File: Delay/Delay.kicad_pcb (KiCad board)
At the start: 2 copper layers, 60 x 110 mm, 64 parts, among them J1 IN, J2 DC IN, J3 OUT, U1 TL072, U2 PT2399, U3 LP2950-5.0_TO252

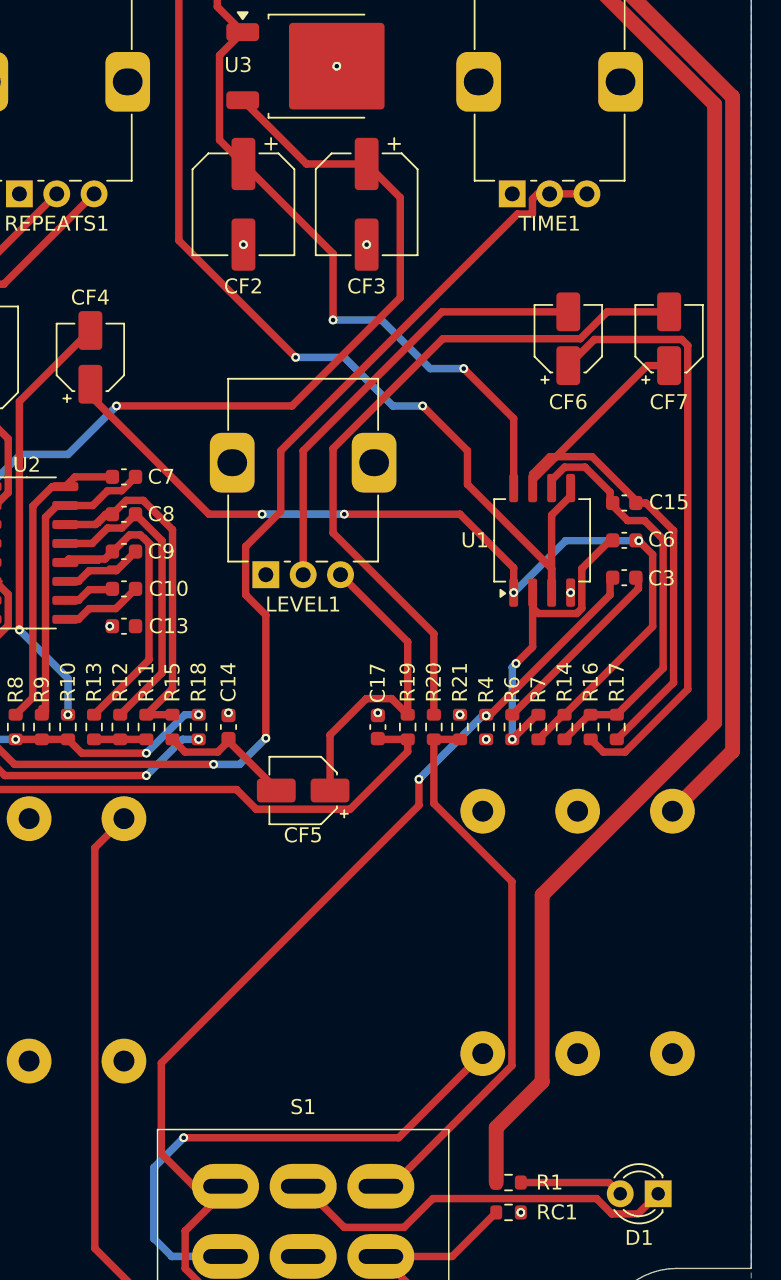
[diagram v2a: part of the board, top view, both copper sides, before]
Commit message: moved input jack to match the x height of the output jack (it was off by 0.5mm)
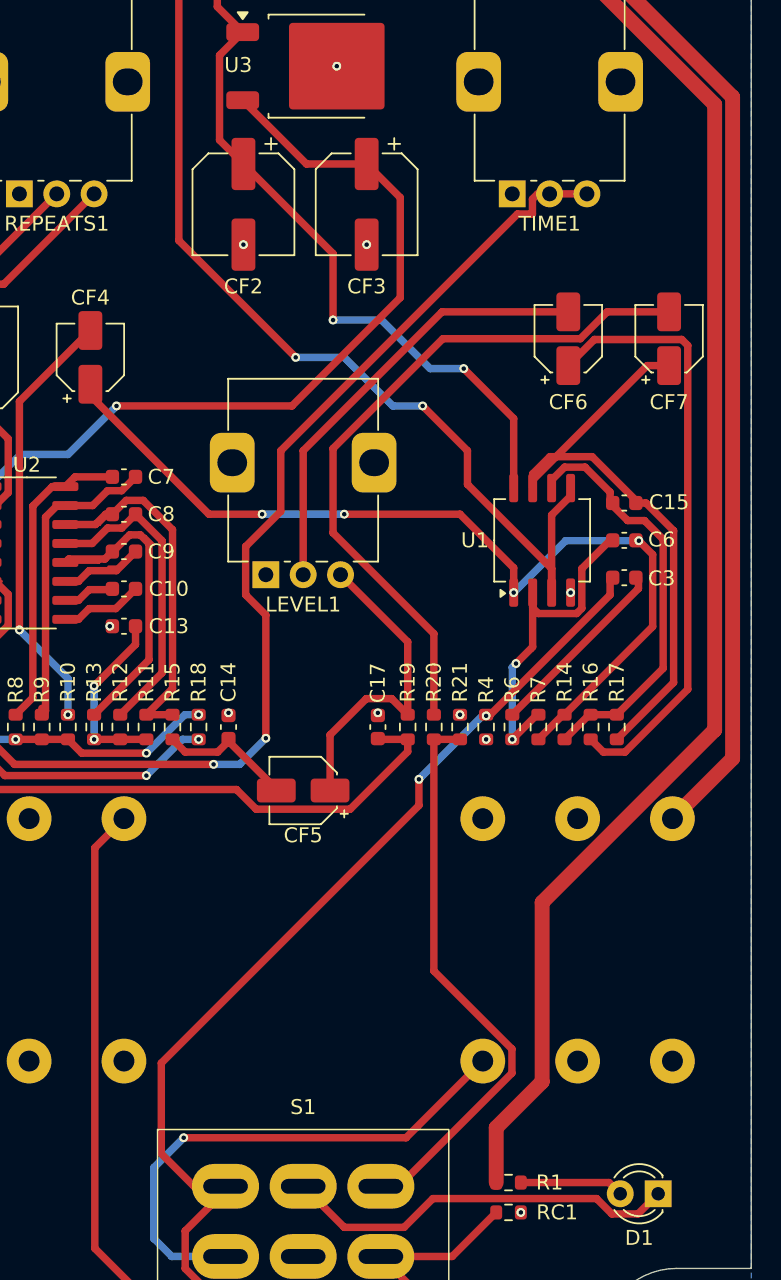
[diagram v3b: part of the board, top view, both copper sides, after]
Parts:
- moved J1 0.50 mm to (162.0, 126.1)
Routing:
- net Net-(C13-Pad1): track 3.50 -> 12.2 mm, vias 0 -> 2
- net Net-(-9VBATT1-Pad1): track 74.2 -> 75.2 mm
- net Wet Out: track 37.2 -> 38.2 mm
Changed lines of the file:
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@@
 	(footprint "Connector_Audio:Jack_6.35mm_Neutrik_NMJ6HFD2_Horizontal"
 		(layer "B.Cu")
-		(at 162.025 125.615)
+		(at 162.025 126.115)
 		(descr "M Series, 6.35mm (1/4in) stereo jack, switched, with full threaded nose and straight PCB pins, https://www.neutrik.com/en/product/nmj6hfd2")
 		(tags "neutrik jack m")
@@
 	)
 	(segment
-		(start 177.551 103.446315)
-		(end 177.551 62.067848)
-		(width 1)
-		(layer "F.Cu")
-		(net 1)
-	)
-	(segment
 		(start 139.999 48.447292)
 		(end 139.999 46.026)
@@
 	)
 	(segment
-		(start 166 127.5)
-		(end 166 114.997315)
-		(width 1)
-		(layer "F.Cu")
-		(net 1)
-	)
-	(segment
 		(start 141.025 45)
 		(end 141.025 42.425)
 		(width 0.5)
+		(layer "F.Cu")
+		(net 1)
+	)
+	(segment
+		(start 153.001 48.551)
+		(end 150 45.55)
+		(width 1)
 		(layer "F.Cu")
 		(net 1)
@@
 	)
 	(segment
+		(start 150 45.55)
+		(end 145.649 41.199)
+		(width 0.5)
+		(layer "F.Cu")
+		(net 1)
+	)
+	(segment
+		(start 139.999 46.026)
+		(end 141.025 45)
+		(width 0.5)
+		(layer "F.Cu")
+		(net 1)
+	)
+	(segment
+		(start 150 45.55)
+		(end 144.25 51.3)
+		(width 0.5)
+		(layer "F.Cu")
+		(net 1)
+	)
+	(segment
 		(start 154.095423 51.751)
 		(end 153.001 50.656577)
@@
 	)
 	(segment
-		(start 150 45.55)
-		(end 145.649 41.199)
-		(width 0.5)
-		(layer "F.Cu")
-		(net 1)
-	)
-	(segment
-		(start 139.999 46.026)
-		(end 141.025 45)
-		(width 0.5)
-		(layer "F.Cu")
-		(net 1)
-	)
-	(segment
-		(start 150 45.55)
-		(end 144.25 51.3)
-		(width 0.5)
+		(start 177.551 62.067848)
+		(end 167.234152 51.751)
+		(width 1)
 		(layer "F.Cu")
 		(net 1)
@@
 		(start 145.649 41.199)
 		(end 141.901 41.199)
-		(width 0.5)
-		(layer "F.Cu")
-		(net 1)
-	)
-	(segment
-		(start 141.051708 49.5)
-		(end 139.999 48.447292)
 		(width 0.5)
 		(layer "F.Cu")
@@
 	)
 	(segment
+		(start 141.051708 49.5)
+		(end 139.999 48.447292)
+		(width 0.5)
+		(layer "F.Cu")
+		(net 1)
+	)
+	(segment
+		(start 177.551 103.946315)
+		(end 166 115.497315)
+		(width 1)
+		(layer "F.Cu")
+		(net 1)
+	)
+	(segment
 		(start 162.925 134.25)
 		(end 162.925 130.575)
@@
 	)
 	(segment
-		(start 166 114.997315)
-		(end 177.551 103.446315)
+		(start 166 115.497315)
+		(end 166 127.5)
 		(width 1)
 		(layer "F.Cu")
@@
 		(start 144.25 51.3)
 		(end 144.25 55.52)
+		(width 0.5)
+		(layer "F.Cu")
+		(net 1)
+	)
+	(segment
+		(start 177.551 62.067848)
+		(end 177.551 103.946315)
+		(width 1)
+		(layer "F.Cu")
+		(net 1)
+	)
+	(segment
+		(start 164.095 87.75)
+		(end 164.095 83.095)
 		(width 0.5)
 		(layer "F.Cu")
@@
 		(net 1)
 	)
-	(segment
-		(start 177.551 62.067848)
-		(end 167.234152 51.751)
-		(width 1)
-		(layer "F.Cu")
-		(net 1)
-	)
-	(segment
-		(start 164.095 87.75)
-		(end 164.095 83.095)
-		(width 0.5)
-		(layer "F.Cu")
-		(net 1)
-	)
-	(segment
-		(start 153.001 48.551)
-		(end 150 45.55)
-		(width 1)
-		(layer "F.Cu")
-		(net 1)
-	)
 	(via
 		(at 160.75 79.75)
@@
 	)
 	(segment
-		(start 156.39 131.25)
-		(end 162.025 125.615)
+		(start 156.89 131.25)
+		(end 162.025 126.115)
 		(width 0.5)
 		(layer "F.Cu")
@@
 	(segment
 		(start 142 131.25)
-		(end 156.39 131.25)
+		(end 156.89 131.25)
 		(width 0.5)
 		(layer "F.Cu")
@@
 	)
 	(segment
-		(start 163.976 126.423131)
-		(end 163.976 114.095131)
+		(start 163.976 125.306869)
+		(end 163.976 126.923131)
 		(width 0.5)
 		(layer "F.Cu")
@@
 	)
 	(segment
-		(start 158.75 108.869131)
-		(end 158.75 104.575)
+		(start 163.976 126.923131)
+		(end 156.399131 134.5)
 		(width 0.5)
 		(layer "F.Cu")
@@
 	)
 	(segment
-		(start 163.976 114.095131)
-		(end 158.75 108.869131)
+		(start 158.75 104.575)
+		(end 158.75 120.080869)
+		(width 0.5)
+		(layer "F.Cu")
+		(net 9)
+	)
+	(segment
+		(start 156.399131 134.5)
+		(end 155.2 134.5)
+		(width 0.5)
+		(layer "F.Cu")
+		(net 9)
+	)
+	(segment
+		(start 158.75 120.080869)
+		(end 163.976 125.306869)
 		(width 0.5)
 		(layer "F.Cu")
@@
 	)
 	(segment
-		(start 155.899131 134.5)
-		(end 163.976 126.423131)
-		(width 0.5)
-		(layer "F.Cu")
-		(net 9)
-	)
-	(segment
 		(start 146.751 145.851)
 		(end 144.8 143.9)
@@
 	)
 	(segment
+		(start 138.775 98.225)
+		(end 138.775 97)
+		(width 0.5)
+		(layer "F.Cu")
+		(net 13)
+	)
+	(segment
+		(start 136 101)
+		(end 138.775 98.225)
+		(width 0.5)
+		(layer "F.Cu")
+		(net 13)
+	)
+	(segment
 		(start 136 104.575)
 		(end 139.5 104.575)
 		(width 0.5)
 		(layer "F.Cu")
+		(net 13)
+	)
+	(via
+		(at 136 104.575)
+		(size 0.6)
+		(drill 0.3)
+		(layers "F.Cu" "B.Cu")
+		(net 13)
+	)
+	(via
+		(at 136 101)
+		(size 0.6)
+		(drill 0.3)
+		(layers "F.Cu" "B.Cu")
+		(net 13)
+	)
+	(segment
+		(start 136 104.575)
+		(end 136 101)
+		(width 0.5)
+		(layer "B.Cu")
 		(net 13)
 	)
@@
 	)
 	(segment
+		(start 174.725 109.385)
+		(end 174.725 109.885)
+		(width 1)
+		(layer "F.Cu")
+		(net 22)
+	)
+	(segment
+		(start 178.752 61.570378)
+		(end 178.752 105.858)
+		(width 1)
+		(layer "F.Cu")
+		(net 22)
+	)
+	(segment
 		(start 159.25 49)
 		(end 166.181622 49)
@@
 	)
 	(segment
-		(start 178.752 61.570378)
-		(end 178.752 105.358)
+		(start 178.752 105.858)
+		(end 174.725 109.885)
 		(width 1)
 		(layer "F.Cu")
-		(net 22)
-	)
-	(segment
-		(start 178.752 105.358)
-		(end 174.725 109.385)
-		(width 1)
-		(layer "F.Cu")

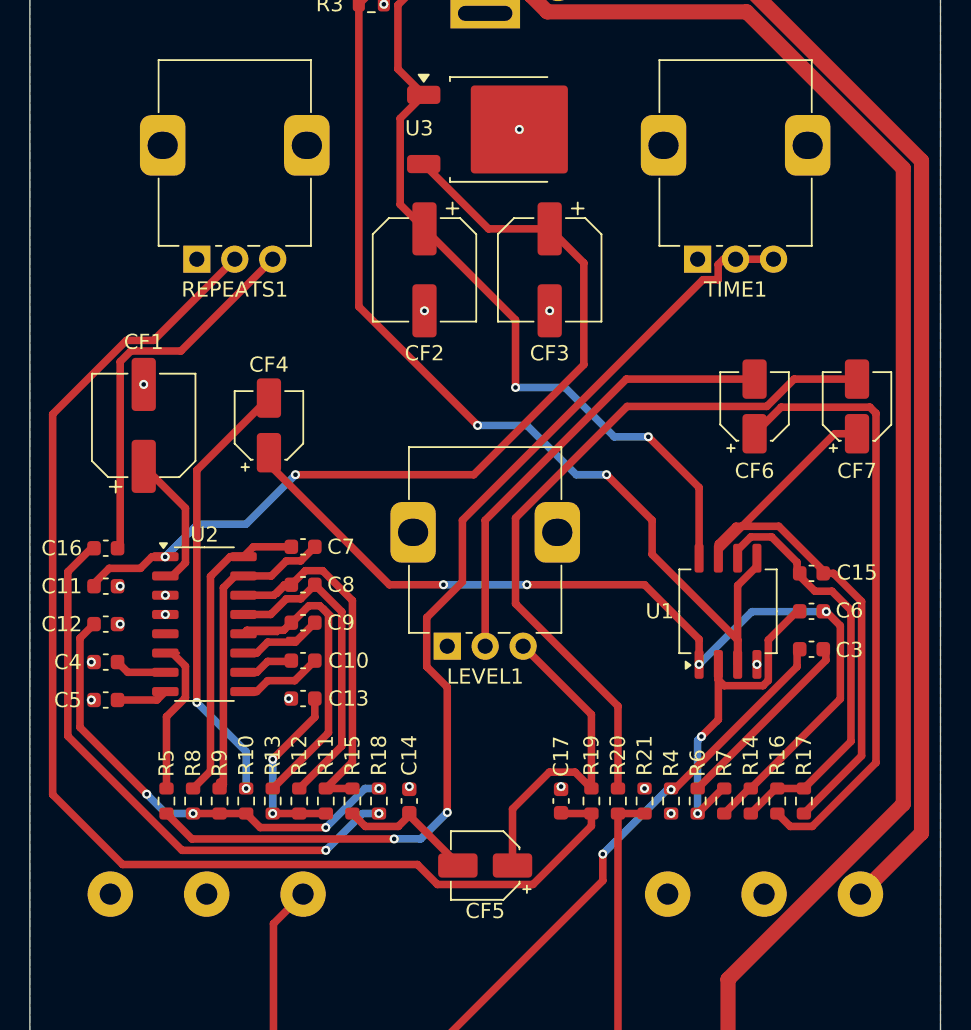
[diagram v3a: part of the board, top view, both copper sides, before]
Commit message: changed caps to be THT and to be sourced separately.
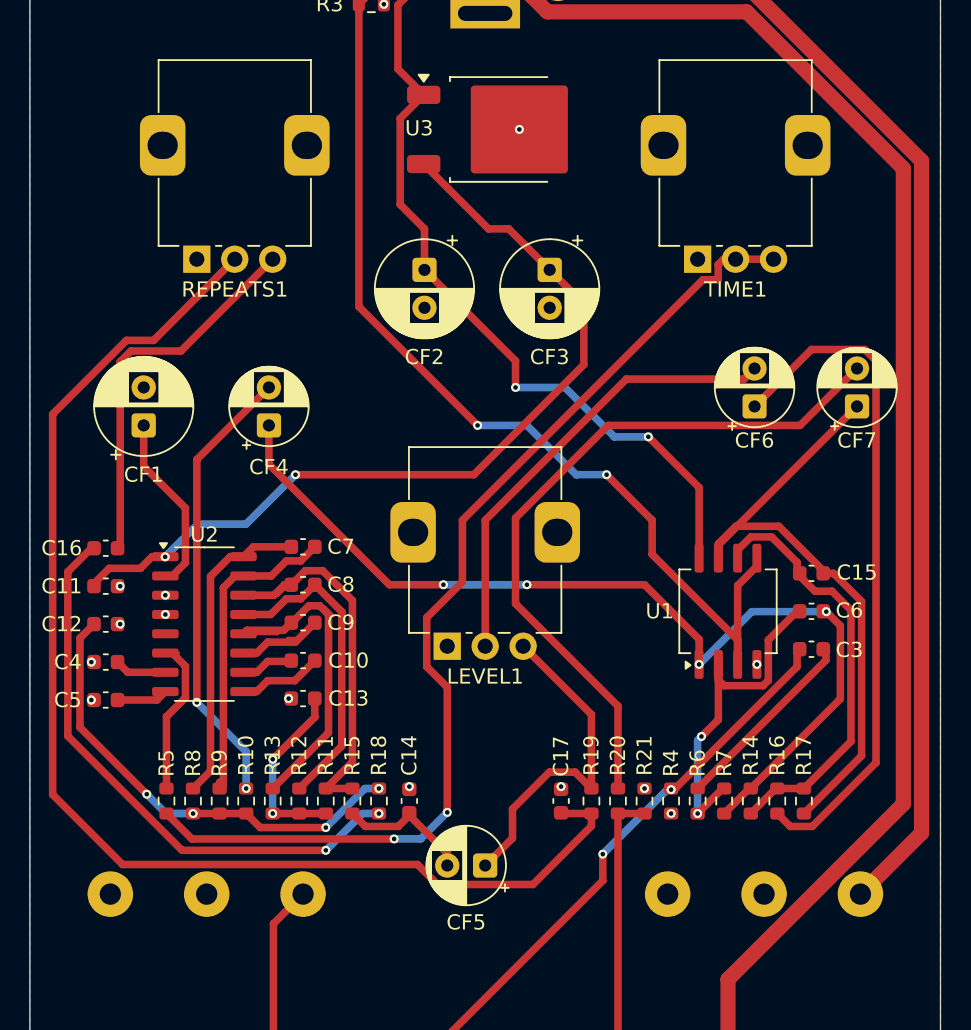
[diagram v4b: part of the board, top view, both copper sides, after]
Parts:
- CF1, CF2, CF3: footprint Capacitor_SMD:CP_Elec_6.3x7.7 -> Capacitor_THT:CP_Radial_D6.3mm_P2.50mm
- CF4, CF5, CF6, CF7: footprint Capacitor_SMD:CP_Elec_4x5.4 -> Capacitor_THT:CP_Radial_D5.0mm_P2.50mm
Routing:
- net Delayed Signal: track 48.7 -> 44.9 mm
- net Net-(U2-REF): track 8.72 -> 11.4 mm
- net Buffered Signal: track 61.4 -> 64.0 mm
- net +5V: track 58.4 -> 56.9 mm
- net Net-(C15-Pad2): track 40.8 -> 41.7 mm
- net Net-(CF5-Pad1): track 21.6 -> 22.4 mm
- net Net-(CF4-Pad2): track 29.0 -> 29.7 mm
- net GND: vias 21 -> 18
